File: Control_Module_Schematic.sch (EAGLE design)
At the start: 17 parts

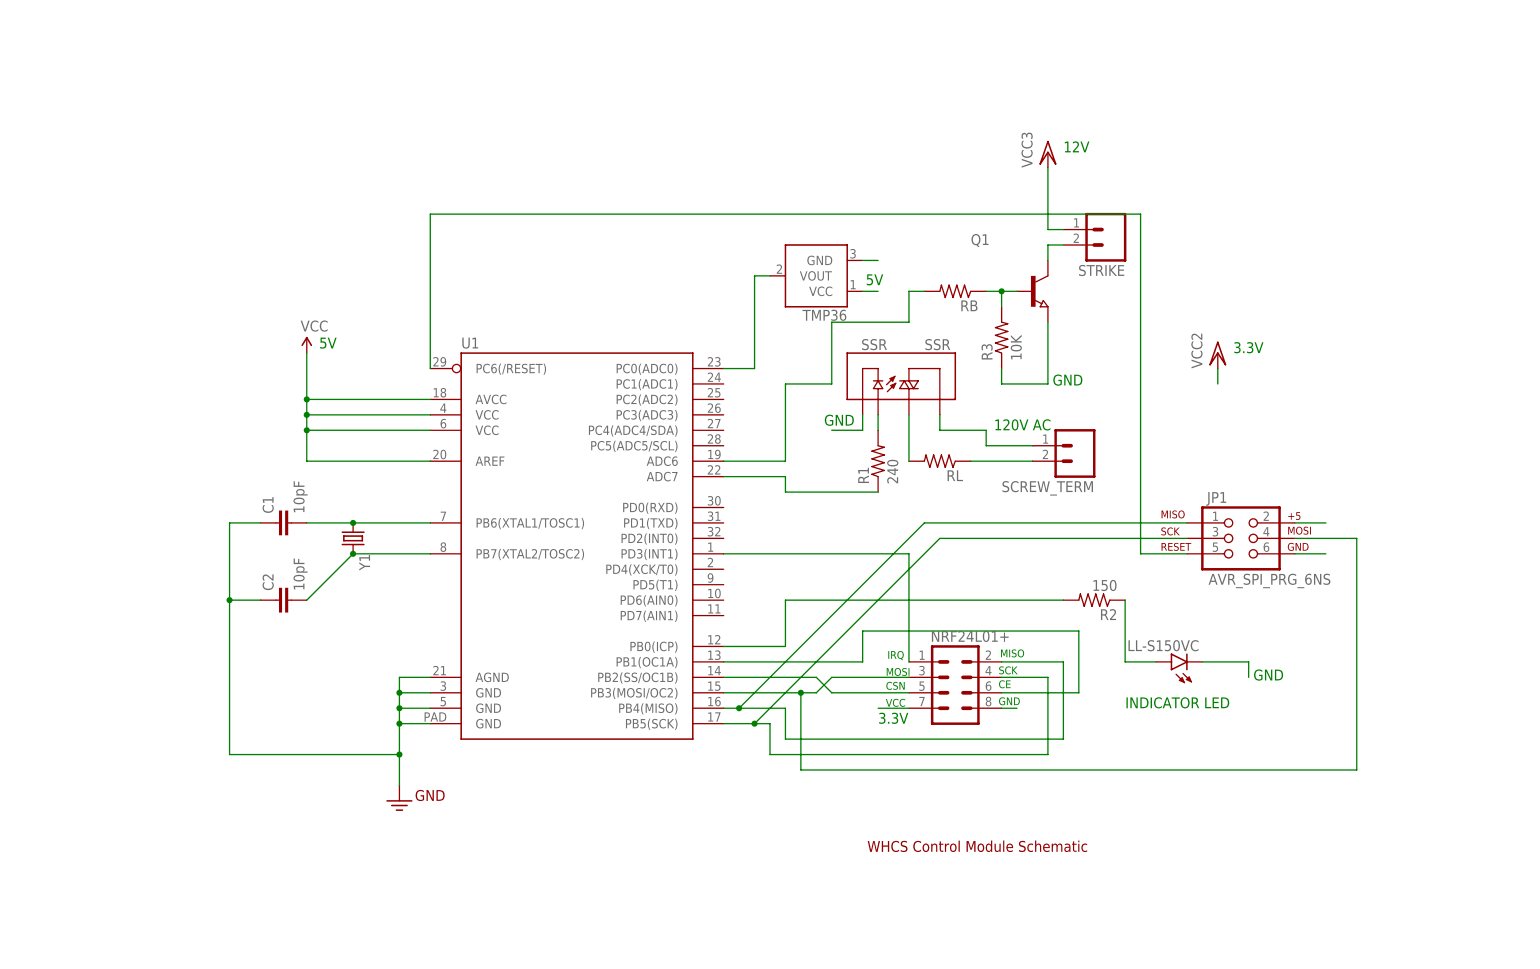
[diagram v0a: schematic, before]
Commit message: Made the layout for the board.
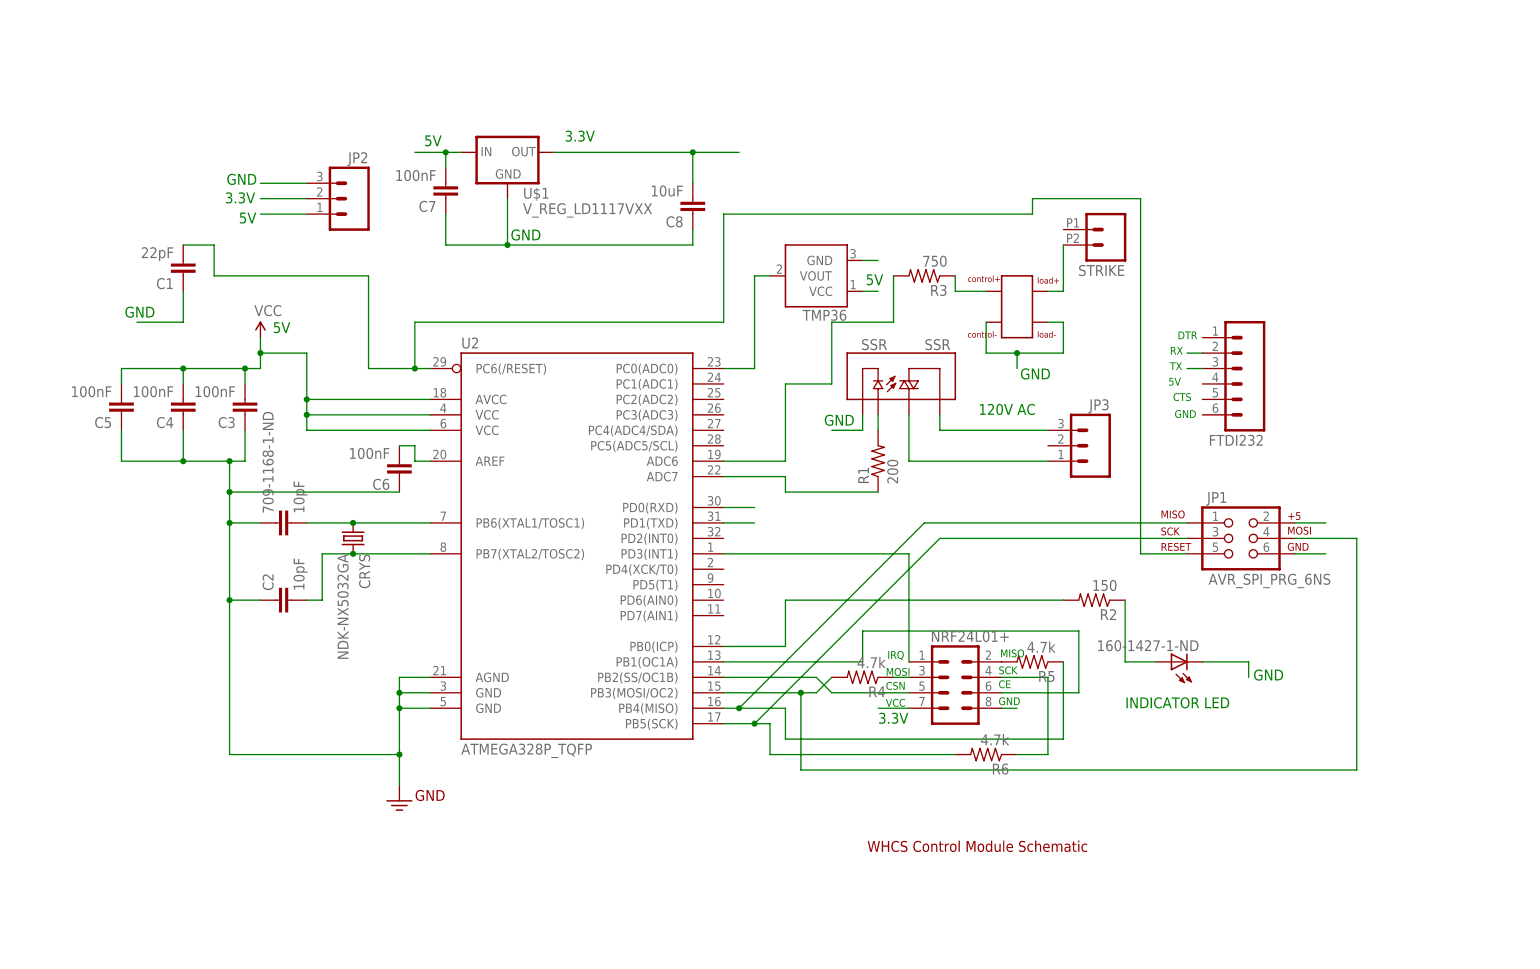
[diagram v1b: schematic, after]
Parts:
- removed LL-S150VC: (no value), SparkFun-LED:LED-FKIT-1206
- removed Q1: (no value), semicon-smd-ipc:NPN-TRANSISTOR_SOT23
- removed RB, RL: (no value), rcl:R-US_R0805
- removed SCREW_TERM: (no value), SparkFun-Connectors:M025MM
- removed U1: (no value), SparkFun-DigitalIC:ATMEGA328P_MLFMLF32
- removed Y1: (no value), SparkFun-FreqCtrl:CRYSTAL10.5X4.8
- added 160-1427-1-ND: (no value), led:LEDCHIP-LED0805
- added 709-1168-1-ND: 10pF, SparkFun-Capacitors:1UF-25V-10%(0805)"
- added C3, C4, C5, C6, C7: 100nF, SparkFun-Capacitors:1UF-25V-10%(0805)"
- added C8: 10uF, SparkFun-Capacitors:1UF-25V-10%(0805)"
- added CPC1002NTR: CPC1002NTR, WHCS:CPC1002NTR
- added CRYS: NDK-NX5032GA, WHCS:NDK-NX5032GA
- added FTDI232: (no value), SparkFun-Connectors:M06LONGPADS
- added JP2, JP3: (no value), SparkFun-Connectors:M03-SCREW-5MM
- added R4, R5, R6: 4.7k, rcl:R-US_R0805
- added U$1: V_REG_LD1117VXX, SparkFun-PowerIC:V_REG_LD1117VXX
- added U2: ATMEGA328P_TQFP, SparkFun-DigitalIC:ATMEGA328P_TQFP
- C1: value 10pF -> 22pF; device SparkFun-Capacitors:12PF-50V-5%(0603) -> SparkFun-Capacitors:1UF-25V-10%(0805)"
- C2: device SparkFun-Capacitors:12PF-50V-5%(0603) -> SparkFun-Capacitors:1UF-25V-10%(0805)"
- R1: value 240 -> 200
- R3: value 10K -> 750
- STRIKE: device SparkFun-Connectors:M025MM -> SparkFun-Connectors:M022.54MM_SCREWTERM
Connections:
- removed net N$12: RL.2, SSR.T2
- new net N$21: NRF24L01+.2, R5.2
- new net N$22: NRF24L01+.4, R6.1
- new net N$23: C6.2, U2.AREF
- new net N$24: C1.2, JP1.5, U2.PC6(/RESET)
- new net RXD: FTDI232.3, U2.PD0(RXD)
- new net TXD: FTDI232.2, U2.PD1(TXD)
- net 3.3V: now also C8.2, JP2.2, U$1.OUT; no longer STRIKE.1
- net 5V: now also C3.2, C4.2, C5.2, C7.2, JP2.1, U$1.IN, U2.AVCC, U2.VCC@4, U2.VCC@6; no longer U1.AREF, U1.AVCC, U1.VCC@4, U1.VCC@6
- net GND: now also 160-1427-1-ND.C, 709-1168-1-ND.1, C3.1, C4.1, C5.1, C6.1, C7.1, C8.1, CPC1002NTR.P$1, CPC1002NTR.P$4, JP2.3, U$1.GND, U2.AGND, U2.GND@3, U2.GND@5; no longer LL-S150VC.C, Q1.E, R3.1, U1.AGND, U1.GND@3, U1.GND@5, U1.GND@PAD
- net N$1: now also U2.PB2(SS/OC1B); no longer U1.PB2(SS/OC1B)
- net N$10: now also JP3.3, SSR.T1; no longer JP1.5, U1.PC6(/RESET)
- net N$11: now also JP3.1, SSR.T2; no longer SCREW_TERM.1, SSR.T1
- net N$13: now also CPC1002NTR.CONTROL+, R3.1; no longer RL.1, SCREW_TERM.2
- net N$14: now also 709-1168-1-ND.2, CRYS.1, U2.PB6(XTAL1/TOSC1); no longer C1.2, U1.PB6(XTAL1/TOSC1), Y1.1
- net N$15: now also CRYS.2, U2.PB7(XTAL2/TOSC2); no longer U1.PB7(XTAL2/TOSC2), Y1.2
- net N$16: now also U2.PB0(ICP); no longer U1.PB0(ICP)
- net N$17: now also 160-1427-1-ND.A; no longer LL-S150VC.A
- net N$18: now also CPC1002NTR.P$3, STRIKE.2; no longer Q1.B, R3.2, RB.1
- net N$19: now also R3.2, U2.ADC6; no longer RB.2, U1.ADC6
- net N$2: now also R5.1, U2.PB4(MISO); no longer NRF24L01+.2, U1.PB4(MISO)
- net N$20: now also NRF24L01+.3, R4.1; no longer Q1.C, STRIKE.2
- net N$3: now also R4.2, U2.PB3(MOSI/OC2); no longer NRF24L01+.3, U1.PB3(MOSI/OC2)
- net N$4: now also R6.2, U2.PB5(SCK); no longer NRF24L01+.4, U1.PB5(SCK)
- net N$5: now also U2.PD3(INT1); no longer U1.PD3(INT1)
- net N$6: now also U2.PB1(OC1A); no longer U1.PB1(OC1A)
- net N$7: now also U2.PC0(ADC0); no longer U1.PC0(ADC0)
- net N$9: now also U2.ADC7; no longer U1.ADC7
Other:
- note added: "CTS"
- note added: "DTR"
- note added: "RX"
- note added: "TX"
- note removed: "12V"
- moved on the sheet: C1, R3

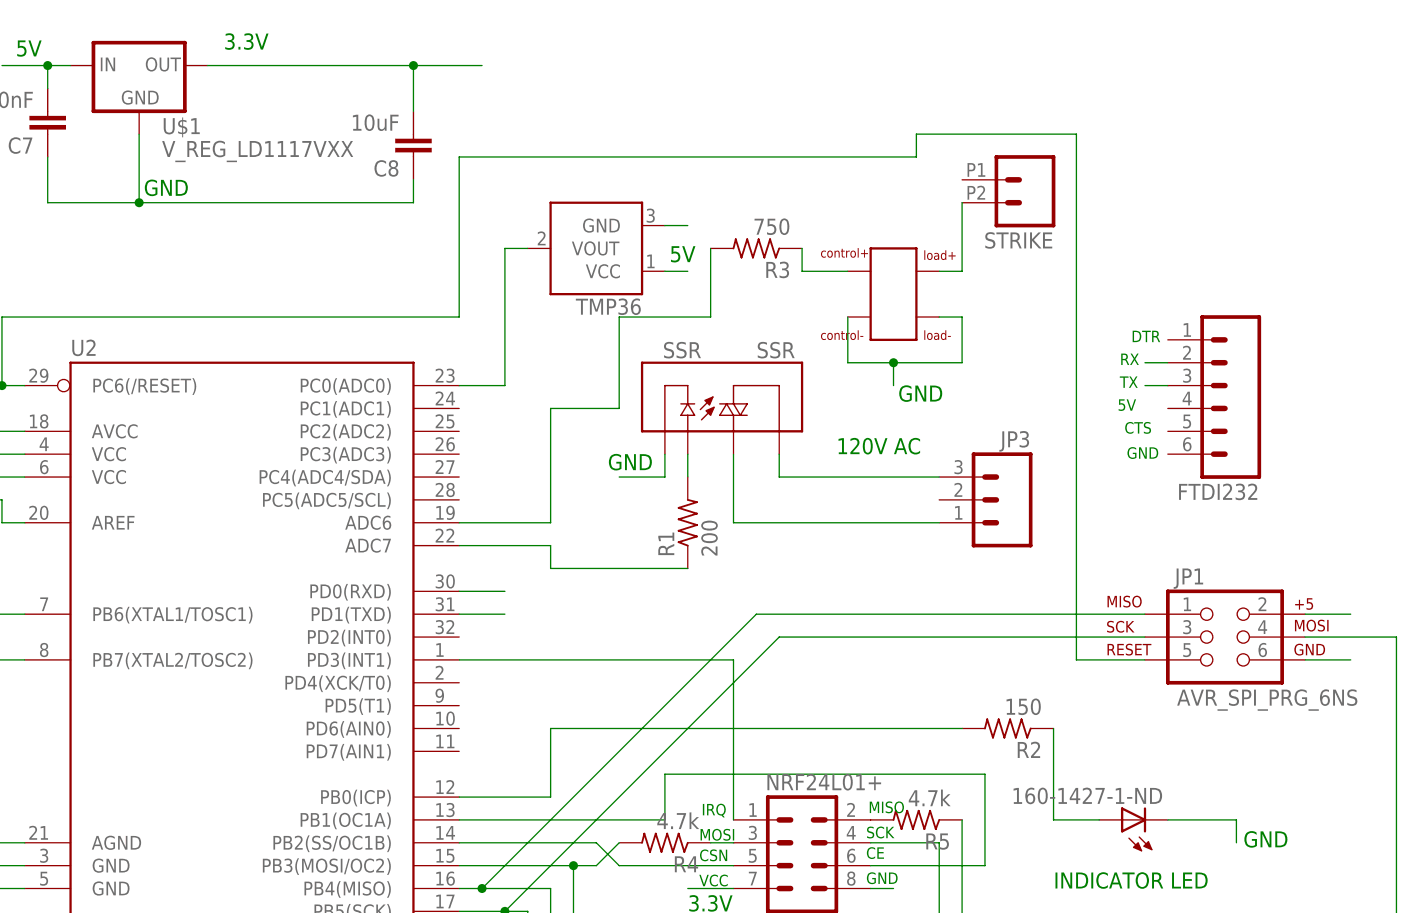
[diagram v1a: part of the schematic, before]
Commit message: Board status when first submitted.
This is the way the board was when first submitted to Oshpark for an
initial run.
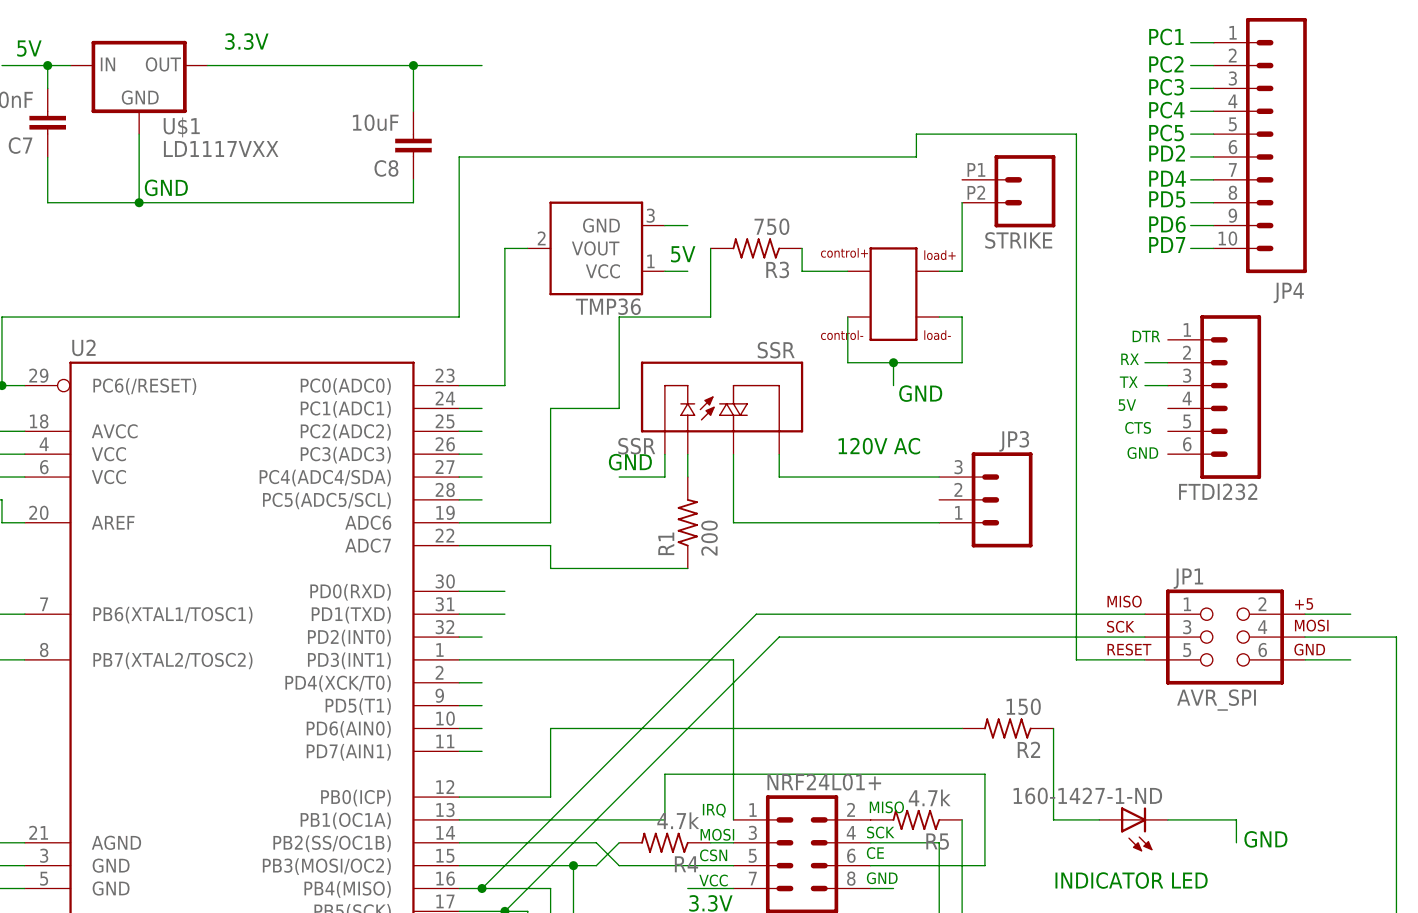
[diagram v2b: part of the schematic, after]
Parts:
- added JP4: (no value), SparkFun-Connectors:M10LOCK_LONGPADS
- JP1: value AVR_SPI_PRG_6NS -> AVR_SPI
- SSR: device SparkFun-Electromechanical:RELAY-SOLIDSTATEPTH -> WHCS:RELAY-SOLIDSTATE
- U$1: value V_REG_LD1117VXX -> LD1117VXX
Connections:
- new net PC1: JP4.1, U2.PC1(ADC1)
- new net PC2: JP4.2, U2.PC2(ADC2)
- new net PC3: JP4.3, U2.PC3(ADC3)
- new net PC4: JP4.4, U2.PC4(ADC4/SDA)
- new net PC5: JP4.5, U2.PC5(ADC5/SCL)
- new net PD2: JP4.6, U2.PD2(INT0)
- new net PD4: JP4.7, U2.PD4(XCK/T0)
- new net PD5: JP4.8, U2.PD5(T1)
- new net PD6: JP4.9, U2.PD6(AIN0)
- new net PD7: JP4.10, U2.PD7(AIN1)
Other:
- note added: "PC1"
- note added: "PC2"
- note added: "PC3"
- note added: "PC4"
- note added: "PC5"
- note added: "PD2"
- note added: "PD4"
- note added: "PD5"
- note added: "PD6"
- note added: "PD7"
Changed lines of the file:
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@@
 </classes>
 <parts>
-<part name="JP1" library="SparkFun-Connectors" deviceset="AVR_SPI_PRG_6" device="NS"/>
+<part name="JP1" library="SparkFun-Connectors" deviceset="AVR_SPI_PRG_6" device="NS" value="AVR_SPI"/>
 <part name="NRF24L01+" library="SparkFun-Connectors" deviceset="M04X2" device=""/>
 <part name="SUPPLY1" library="SparkFun-Aesthetics" deviceset="VCC" device=""/>
 <part name="GND" library="SparkFun-Aesthetics" deviceset="GND2" device=""/>
 <part name="TMP36" library="SparkFun-Sensors" deviceset="TMP36" device="TO-92-KIT"/>
-<part name="SSR" library="SparkFun-Electromechanical" deviceset="RELAY-SOLIDSTATE" device="PTH" value="SSR"/>
+<part name="SSR" library="WHCS" deviceset="RELAY-SOLIDSTATE" device="" value="SSR"/>
 <part name="R1" library="rcl" deviceset="R-US_" device="R0805" value="200"/>
 <part name="CRYS" library="WHCS" deviceset="NDK-NX5032GA" device=""/>
@@
 <part name="C6" library="SparkFun-Capacitors" deviceset="1UF-25V-10%(0805)" device="&quot;" value="100nF"/>
 <part name="U2" library="SparkFun-DigitalIC" deviceset="ATMEGA328P_TQFP" device="" value="ATMEGA328P_TQFP"/>
-<part name="U$1" library="SparkFun-PowerIC" deviceset="V_REG_LD1117VXX" device=""/>
+<part name="U$1" library="SparkFun-PowerIC" deviceset="V_REG_LD1117VXX" device="" value="LD1117VXX"/>
 <part name="C7" library="SparkFun-Capacitors" deviceset="1UF-25V-10%(0805)" device="&quot;" value="100nF"/>
 <part name="C8" library="SparkFun-Capacitors" deviceset="1UF-25V-10%(0805)" device="&quot;" value="10uF"/>
 <part name="JP3" library="SparkFun-Connectors" deviceset="M03" device="-SCREW-5MM"/>
+<part name="JP4" library="SparkFun-Connectors" deviceset="M10" device="LOCK_LONGPADS"/>
 </parts>
 <sheets>
@@
 <text x="-31.242" y="62.738" size="1.778" layer="91">3.3V</text>
 <text x="-54.356" y="61.976" size="1.778" layer="91">5V</text>
+<text x="71.374" y="63.246" size="1.778" layer="91">PC1</text>
+<text x="71.374" y="60.198" size="1.778" layer="91">PC2</text>
+<text x="71.374" y="57.658" size="1.778" layer="91">PC3</text>
+<text x="71.374" y="55.118" size="1.778" layer="91">PC4</text>
+<text x="71.374" y="52.578" size="1.778" layer="91">PC5</text>
+<text x="71.374" y="50.292" size="1.778" layer="91">PD2</text>
+<text x="71.374" y="47.498" size="1.778" layer="91">PD4</text>
+<text x="71.374" y="45.212" size="1.778" layer="91">PD5</text>
+<text x="71.374" y="42.418" size="1.778" layer="91">PD6</text>
+<text x="71.374" y="40.132" size="1.778" layer="91">PD7</text>
 </plain>
 <instances>
@@
 <instance part="C8" gate="G$1" x="-10.16" y="53.34" rot="R180"/>
 <instance part="JP3" gate="G$1" x="55.88" y="12.7" rot="MR0"/>
+<instance part="JP4" gate="G$1" x="88.9" y="45.72" rot="R180"/>
 </instances>
 <busses>
@@
 </segment>
 </net>
+<net name="PC1" class="0">
+<segment>
+<pinref part="JP4" gate="G$1" pin="1"/>
+<wire x1="78.74" y1="63.5" x2="76.2" y2="63.5" width="0.1524" layer="91"/>
+</segment>
+<segment>
+<pinref part="U2" gate="U$1" pin="PC1(ADC1)"/>
+<wire x1="-5.08" y1="22.86" x2="-2.54" y2="22.86" width="0.1524" layer="91"/>
+</segment>
+</net>
+<net name="PC2" class="0">
+<segment>
+<pinref part="JP4" gate="G$1" pin="2"/>
+<wire x1="78.74" y1="60.96" x2="76.2" y2="60.96" width="0.1524" layer="91"/>
+</segment>
+<segment>
+<pinref part="U2" gate="U$1" pin="PC2(ADC2)"/>
+<wire x1="-5.08" y1="20.32" x2="-2.54" y2="20.32" width="0.1524" layer="91"/>
+</segment>
+</net>
+<net name="PC3" class="0">
+<segment>
+<pinref part="JP4" gate="G$1" pin="3"/>
+<wire x1="78.74" y1="58.42" x2="76.2" y2="58.42" width="0.1524" layer="91"/>
+</segment>
+<segment>
+<pinref part="U2" gate="U$1" pin="PC3(ADC3)"/>
+<wire x1="-5.08" y1="17.78" x2="-2.54" y2="17.78" width="0.1524" layer="91"/>
+</segment>
+</net>
+<net name="PC4" class="0">
+<segment>
+<pinref part="JP4" gate="G$1" pin="4"/>
+<wire x1="78.74" y1="55.88" x2="76.2" y2="55.88" width="0.1524" layer="91"/>
+</segment>
+<segment>
+<pinref part="U2" gate="U$1" pin="PC4(ADC4/SDA)"/>
+<wire x1="-5.08" y1="15.24" x2="-2.54" y2="15.24" width="0.1524" layer="91"/>
+</segment>
+</net>
+<net name="PC5" class="0">
+<segment>
+<pinref part="JP4" gate="G$1" pin="5"/>
+<wire x1="78.74" y1="53.34" x2="76.2" y2="53.34" width="0.1524" layer="91"/>
+</segment>
+<segment>
+<pinref part="U2" gate="U$1" pin="PC5(ADC5/SCL)"/>
+<wire x1="-5.08" y1="12.7" x2="-2.54" y2="12.7" width="0.1524" layer="91"/>
+</segment>
+</net>
+<net name="PD2" class="0">
+<segment>
+<pinref part="JP4" gate="G$1" pin="6"/>
+<wire x1="78.74" y1="50.8" x2="76.2" y2="50.8" width="0.1524" layer="91"/>
+</segment>
+<segment>
+<pinref part="U2" gate="U$1" pin="PD2(INT0)"/>
+<wire x1="-5.08" y1="-2.54" x2="-2.54" y2="-2.54" width="0.1524" layer="91"/>
+</segment>
+</net>
+<net name="PD4" class="0">
+<segment>
+<pinref part="JP4" gate="G$1" pin="7"/>
+<wire x1="78.74" y1="48.26" x2="76.2" y2="48.26" width="0.1524" layer="91"/>
+</segment>
+<segment>
+<pinref part="U2" gate="U$1" pin="PD4(XCK/T0)"/>
+<wire x1="-5.08" y1="-7.62" x2="-2.54" y2="-7.62" width="0.1524" layer="91"/>
+</segment>
+</net>
+<net name="PD5" class="0">
+<segment>
+<pinref part="JP4" gate="G$1" pin="8"/>
+<wire x1="78.74" y1="45.72" x2="76.2" y2="45.72" width="0.1524" layer="91"/>
+</segment>
+<segment>
+<pinref part="U2" gate="U$1" pin="PD5(T1)"/>
+<wire x1="-5.08" y1="-10.16" x2="-2.54" y2="-10.16" width="0.1524" layer="91"/>
+</segment>
+</net>
+<net name="PD6" class="0">
+<segment>
+<pinref part="JP4" gate="G$1" pin="9"/>
+<wire x1="78.74" y1="43.18" x2="76.2" y2="43.18" width="0.1524" layer="91"/>
+</segment>
+<segment>
+<pinref part="U2" gate="U$1" pin="PD6(AIN0)"/>
+<wire x1="-5.08" y1="-12.7" x2="-2.54" y2="-12.7" width="0.1524" layer="91"/>
+</segment>
+</net>
+<net name="PD7" class="0">
+<segment>
+<pinref part="JP4" gate="G$1" pin="10"/>
+<wire x1="78.74" y1="40.64" x2="76.2" y2="40.64" width="0.1524" layer="91"/>
+</segment>
+<segment>
+<pinref part="U2" gate="U$1" pin="PD7(AIN1)"/>
+<wire x1="-5.08" y1="-15.24" x2="-2.54" y2="-15.24" width="0.1524" layer="91"/>
+</segment>
+</net>
